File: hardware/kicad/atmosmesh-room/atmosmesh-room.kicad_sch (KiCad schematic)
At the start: 32 parts, among them U1 IDEASPARK_ESP32_1V14_TFT_30PIN

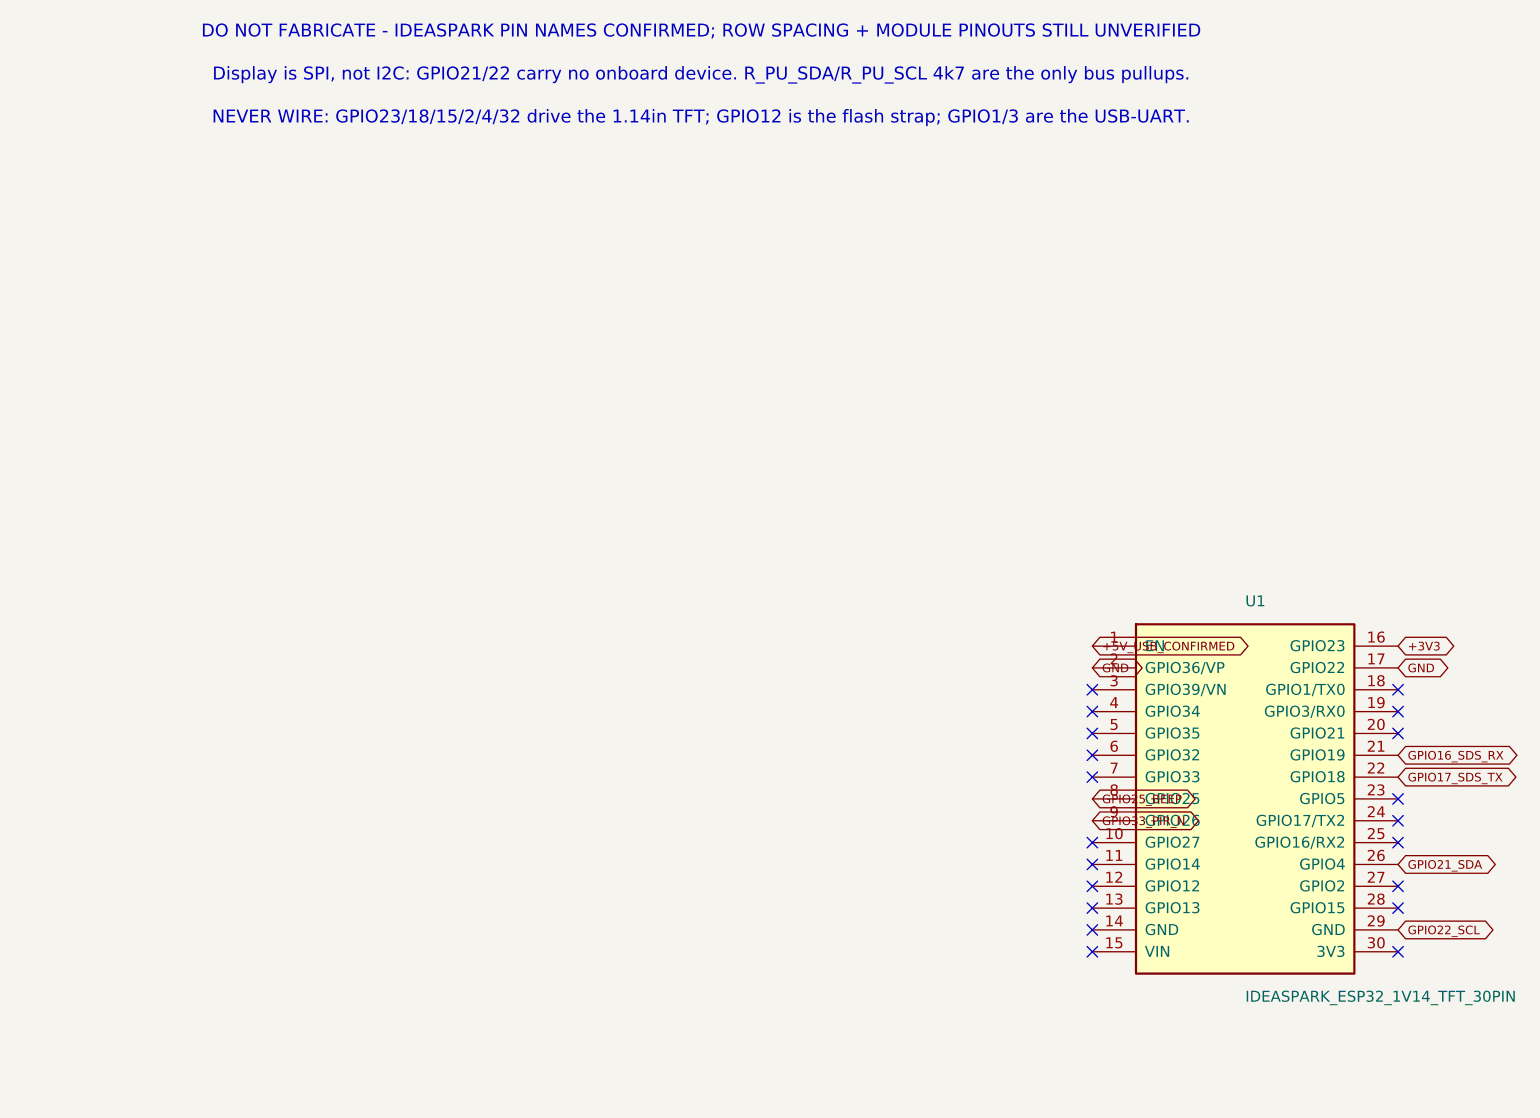
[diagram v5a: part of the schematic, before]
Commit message: :bug: fix(room): stop the schematic labelling the TFT pins as power rails
Final review of the generated artifacts. U1's nets were right, but its symbol
was still the bench project's ESP32_DevKit_V1_Socket, whose pin names run from
the opposite end of the row. KiCad writes each unconnected pad's own pin name
into a placeholder net, which is where this surfaced:

  pad 30  showed 3V3     - it is really GPIO23, the TFT MOSI line
  pad  4  showed GPIO34  - it is really GPIO12, the flash-voltage strap

That is precisely the hazard D-024 names: knowing the pin order makes the
socket more dangerous, because a builder can now confidently reach the wrong
pin. A schematic that prints "3V3" next to TFT MOSI is worse than a provisional
one that admits it does not know.

The symbol is renamed to Ideaspark_ESP32_1V14_TFT_30Pin and every pin relabelled
from IDEASPARK_PINS. Renaming needed three coordinated edits or KiCad refuses to
load the sheet at all: the entry name, each unit's own entry name, and the
library's default Value property.

The validator now refuses the DevKit name and asserts pads 30, 24, 4 and 10 are
labelled GPIO23/GPIO18/GPIO12/GPIO32 and left unconnected. Both mutation-proved:
relabelling pad 30 back to 3V3 fails, and connecting pad 24 fails.

Also completes the Zener inventory from the operator: 1N4733 through 1N4748.
The lowest is still 5.1 V and no 1N4728 is held, so the no-Zener rule now rests
on a complete list. Stale "60x80 mm" and "photos first" language cleared from
wiring.md and the silkscreen, since the build target is perfboard.

Gates: ERC 0, DRC 0 violations and 0 parity problems, both validators PASS,
git diff --check clean.
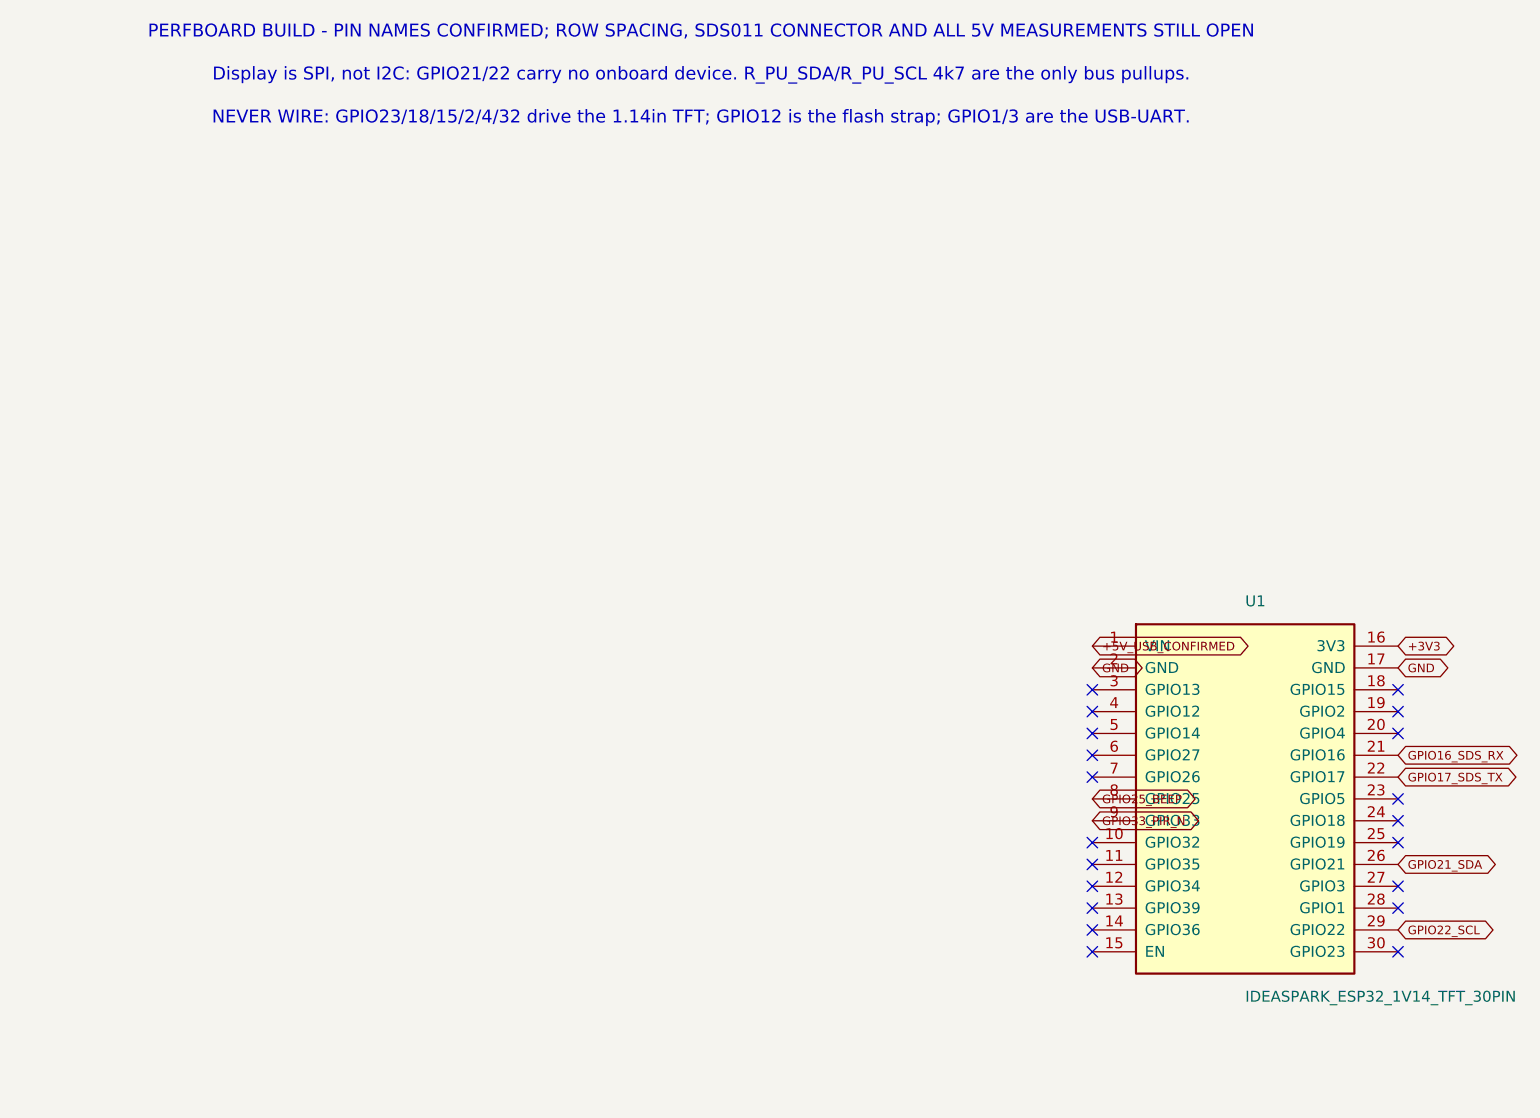
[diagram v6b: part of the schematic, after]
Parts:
- U1: symbol atmosmesh:ESP32_DevKit_V1_Socket -> atmosmesh:Ideaspark_ESP32_1V14_TFT_30Pin
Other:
- note added: "PERFBOARD BUILD - PIN NAMES CONFIRMED; ROW SPACING, SDS011 CONNECTOR AND ALL 5V MEASUREMENTS STILL OPEN"
- note removed: "DO NOT FABRICATE - IDEASPARK PIN NAMES CONFIRMED; ROW SPACING + MODULE PINOUTS STILL UNVERIFIED"
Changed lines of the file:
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@@
     (rev "PROVISIONAL A")
     (company "AtmosMesh")
-    (comment 1 "DO NOT FABRICATE - Ideaspark pin names confirmed; row spacing and module pinouts still unverified")
+    (comment 1 "DO NOT ENERGISE - row spacing, SDS011 connector order and all 5 V measurements still open")
     (comment 2 "GPIO21 SDA / GPIO22 SCL; no 5 V on any GPIO or 3V3")
-    (comment 3 "60x80 mm two-layer THT carrier")
-    (comment 4 "ROOM-01")
+    (comment 3 "Built by hand on a 31x27 perfboard; the PCB is parked")
+    (comment 4 "ROOM-01 / 02 / 03")
   )
   (no_connect (at 63.5 91.44))
@@
   (no_connect (at 99.06 121.92))
   (no_connect (at 137.16 43.18))
-  (text "DO NOT FABRICATE - IDEASPARK PIN NAMES CONFIRMED; ROW SPACING + MODULE PINOUTS STILL UNVERIFIED"
+  (text "PERFBOARD BUILD - PIN NAMES CONFIRMED; ROW SPACING, SDS011 CONNECTOR AND ALL 5V MEASUREMENTS STILL OPEN"
     (at 18 15 0)
     (effects (font (size 1.5 1.5)))
@@
     (effects (font (size 1.0 1.0)))
   )
-  (symbol (lib_id "atmosmesh:ESP32_DevKit_V1_Socket") (at 81.28 104.14 0) (unit 1)
+  (symbol (lib_id "atmosmesh:Ideaspark_ESP32_1V14_TFT_30Pin") (at 81.28 104.14 0) (unit 1)
     (in_bom yes) (on_board yes) (dnp no)
     (property "Reference" "U1" (at 81.28 81.14 0)

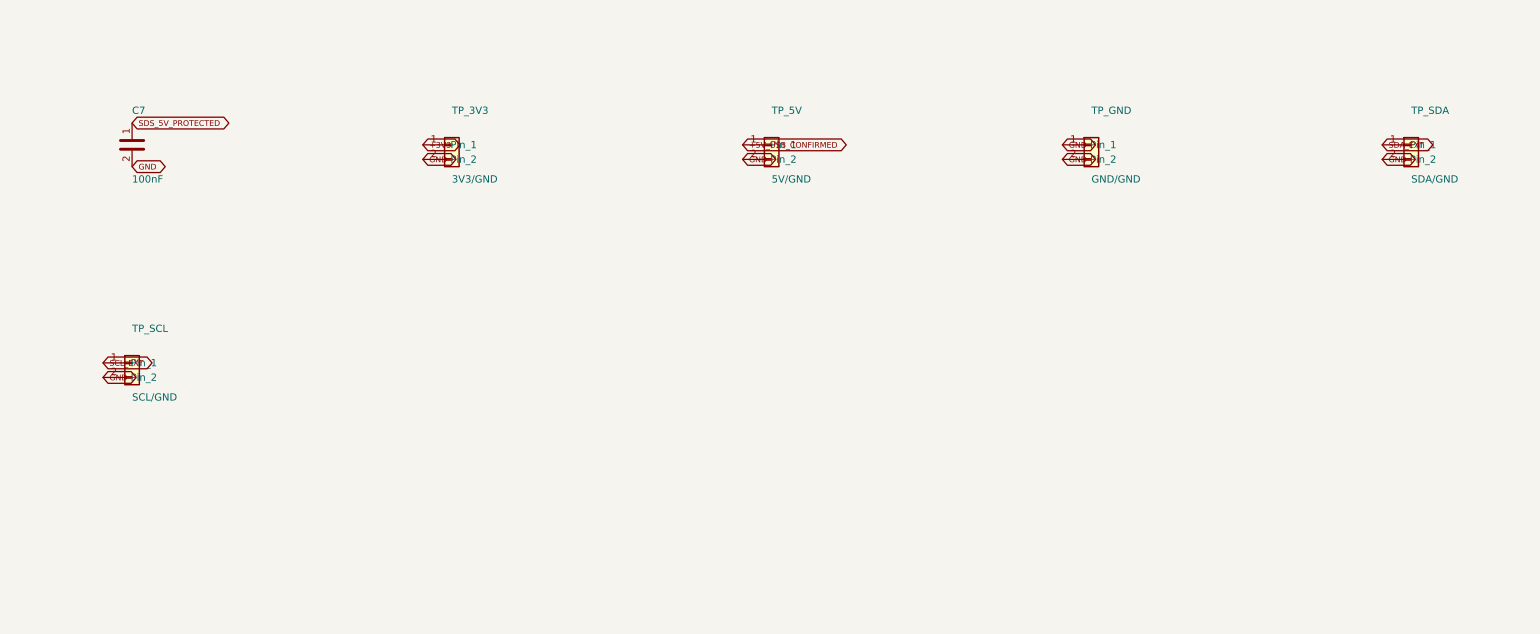
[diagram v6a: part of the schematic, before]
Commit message: :sparkles: feat(room): indicate live domains, and delete the switch the sensor makes unnecessary
Two improvements from the updated inventory, and one of them removes hardware
rather than adding it.

Domain indicators (D-029). Both 5 V jumpers are default-open and the build plan
requires them to stay open until measurements are recorded, but there was no way
to see whether a domain was live - on the one board in this project whose whole
risk story is an unverified 5 V rail. D_LED_3V3 (470R), D_LED_SDS and D_LED_PIR
(1k each) fix that. The 5 V indicators are fed downstream of their own jumpers,
so a lit LED is direct evidence that the jumper it reports on is closed. Red or
green only: a blue LED's ~3.0 V drop leaves 0.6 mA on the 3.3 V rail and reads
as dead.

ROOM-04 rewritten, and D-030 records why. It proposed an IRLZ34N low-side switch
to duty-cycle the SDS011 laser. That was wrong twice:

- The topology does not work. A low-side switch opens the ground return while
  VCC stays at 5 V, so the load is not de-powered - its ground floats up until
  current stops and the sensor sits partially biased. De-powering needs
  high-side switching and no P-channel part is in stock.
- It is unnecessary. nova-sds011.pdf lists "Manual hibernation" and "Timed
  hibernate (Cycle to work)" under Extended functionality, with sleep current
  under 4 mA annotated "Lase&Fan sleep". The sensor duty-cycles itself, and the
  operator's hard-wired TX leg already carries the command.

The parasitic path the old story worried about - TX2 idling HIGH into an
unpowered sensor - disappears with the switch. ROOM-04 is now a firmware story,
gated on obtaining Nova's separate control-protocol document rather than
guessing frame formats at a sensor.

Inventory also gains the HANTEK DSO2D15, IC sockets and heat shrink. The scope
matters: the SDS011 20 mV ripple check was written as "measure with an
oscilloscope" with no instrument on record, and the same tool can settle the
~200 pF bus-capacitance a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
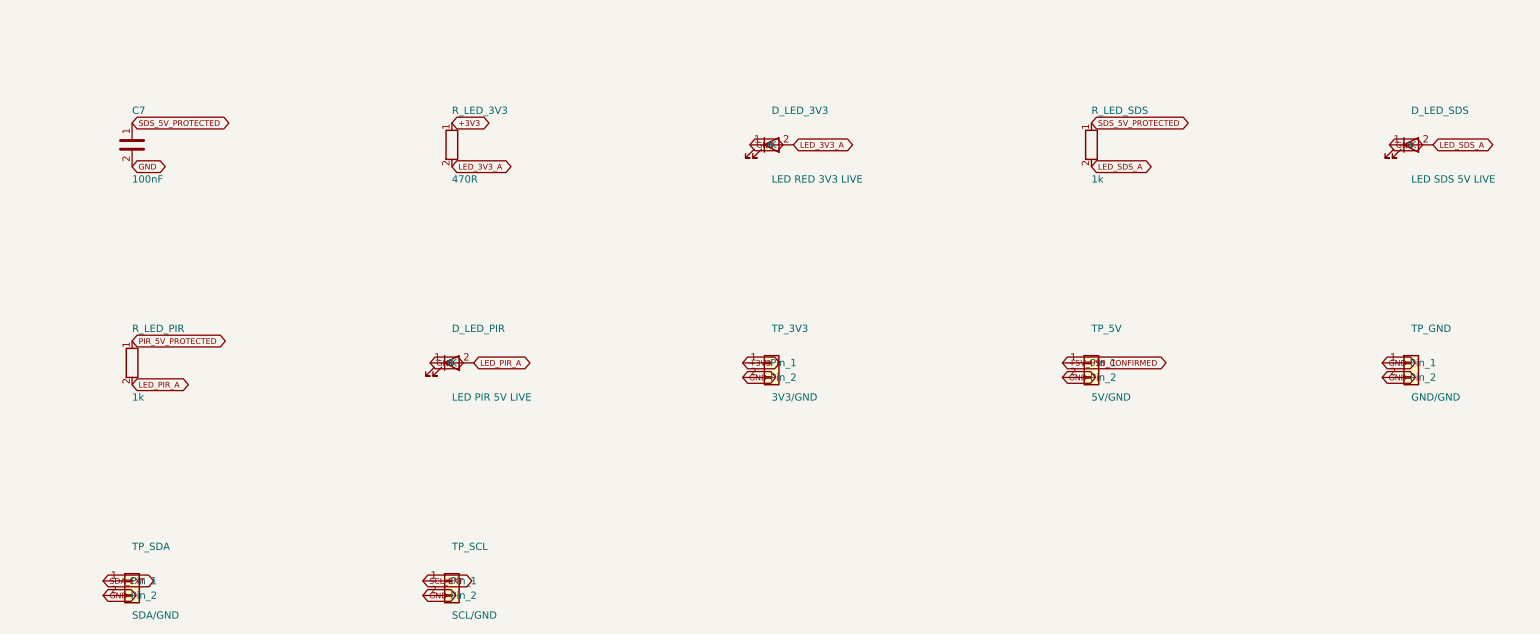
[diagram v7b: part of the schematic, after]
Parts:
- added D_LED_3V3: LED RED 3V3 LIVE, room:D_Axial_P7.62mm, symbol atmosmesh:LED
- added D_LED_PIR: LED PIR 5V LIVE, room:D_Axial_P7.62mm, symbol atmosmesh:LED
- added D_LED_SDS: LED SDS 5V LIVE, room:D_Axial_P7.62mm, symbol atmosmesh:LED
- added R_LED_3V3: 470R, room:R_Axial_P7.62mm, symbol atmosmesh:R
- added R_LED_PIR, R_LED_SDS: 1k, room:R_Axial_P7.62mm, symbol atmosmesh:R
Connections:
- net +3V3: now also R_LED_3V3.1
- net GND: now also D_LED_3V3.1 (K), D_LED_PIR.1 (K), D_LED_SDS.1 (K)
- net PIR_5V_PROTECTED: now also R_LED_PIR.1
- net SDS_5V_PROTECTED: now also R_LED_SDS.1
- new net LED_3V3_A: D_LED_3V3.2 (A), R_LED_3V3.2
- new net LED_PIR_A: D_LED_PIR.2 (A), R_LED_PIR.2
- new net LED_SDS_A: D_LED_SDS.2 (A), R_LED_SDS.2
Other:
- moved on the sheet: TP_3V3, TP_5V, TP_GND, TP_SCL, TP_SDA
